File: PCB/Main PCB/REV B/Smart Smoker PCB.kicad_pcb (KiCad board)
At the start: 4 copper layers, 6.3 x 2.1 mm, 152 parts, among them J1 393570002, J10 Spare2, J2 Conn_01x03_Female, J3 1051330001, J4 Hopper, J5 393570002, J6 393570002, J7 Screen, J8 393570002, J9 Spare1, Q1 2N7002, Q2 2N7002, Q3 MBT3904DW1, Q4 2N7002, U1 AMS1117-3.3, U10 ALDP105W, U11 TLP2362TPR_E, U12 ALDP105W, U13 STM811SW16F, U2 TS5A23159DGS, U3 ESP32-WROOM-32UE_16MB, U4 MAX31855KASA, U5 TPS2115APWR, U6 TLP2362TPR_E, U7 ALDP105W, U8 CP2102N-A02-GQFN24, U9 TLP2362TPR_E

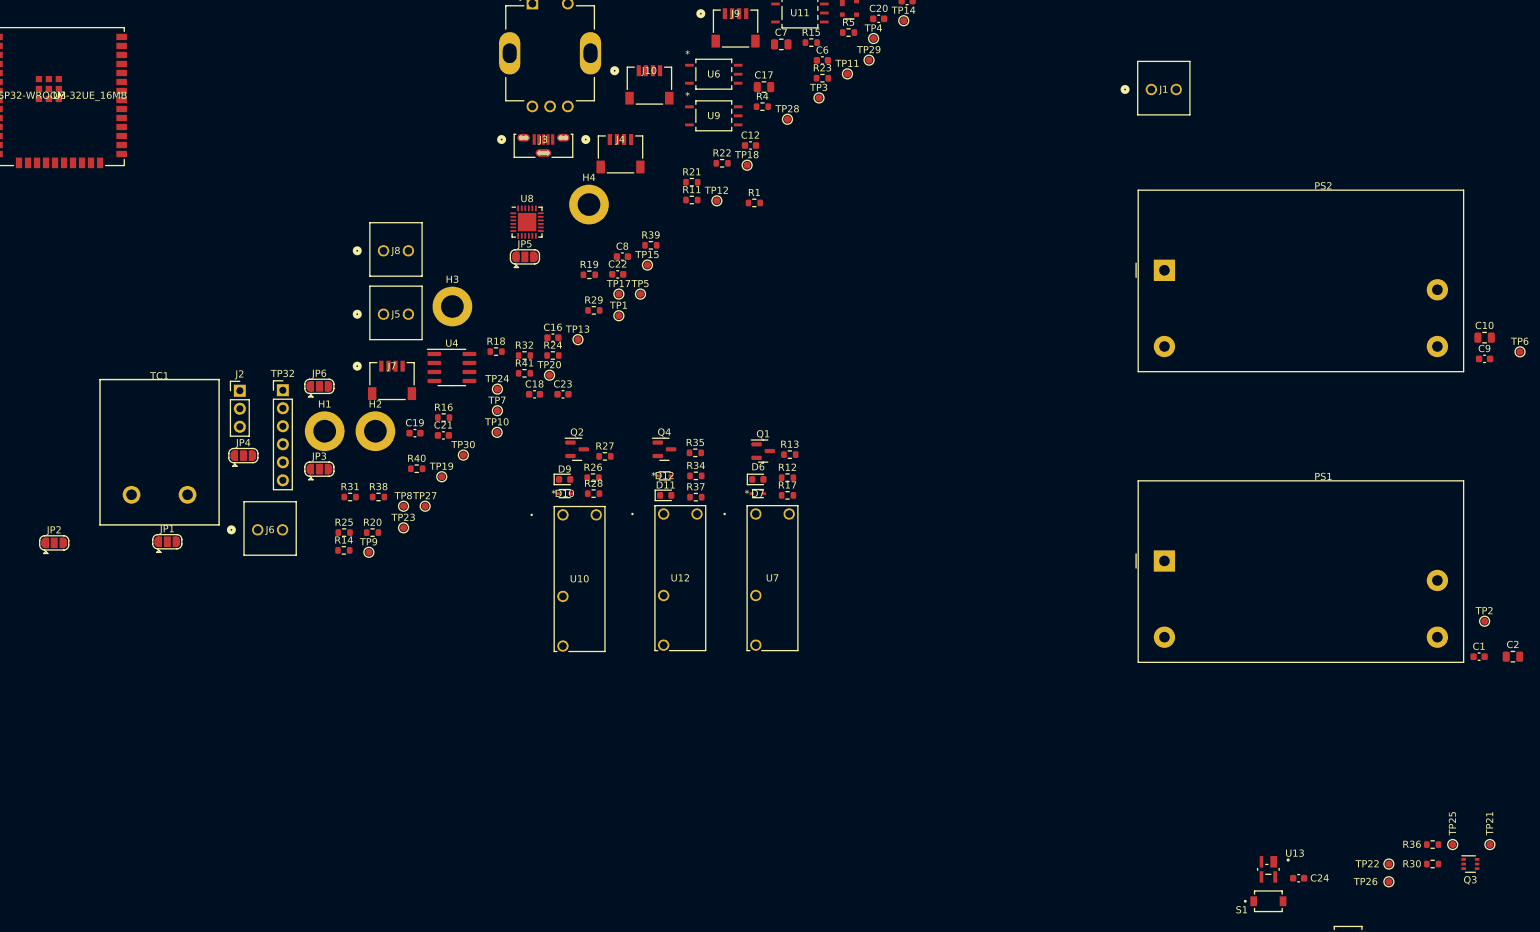
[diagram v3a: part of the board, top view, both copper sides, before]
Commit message: PCB Layout - Continue Grouping layout for relays
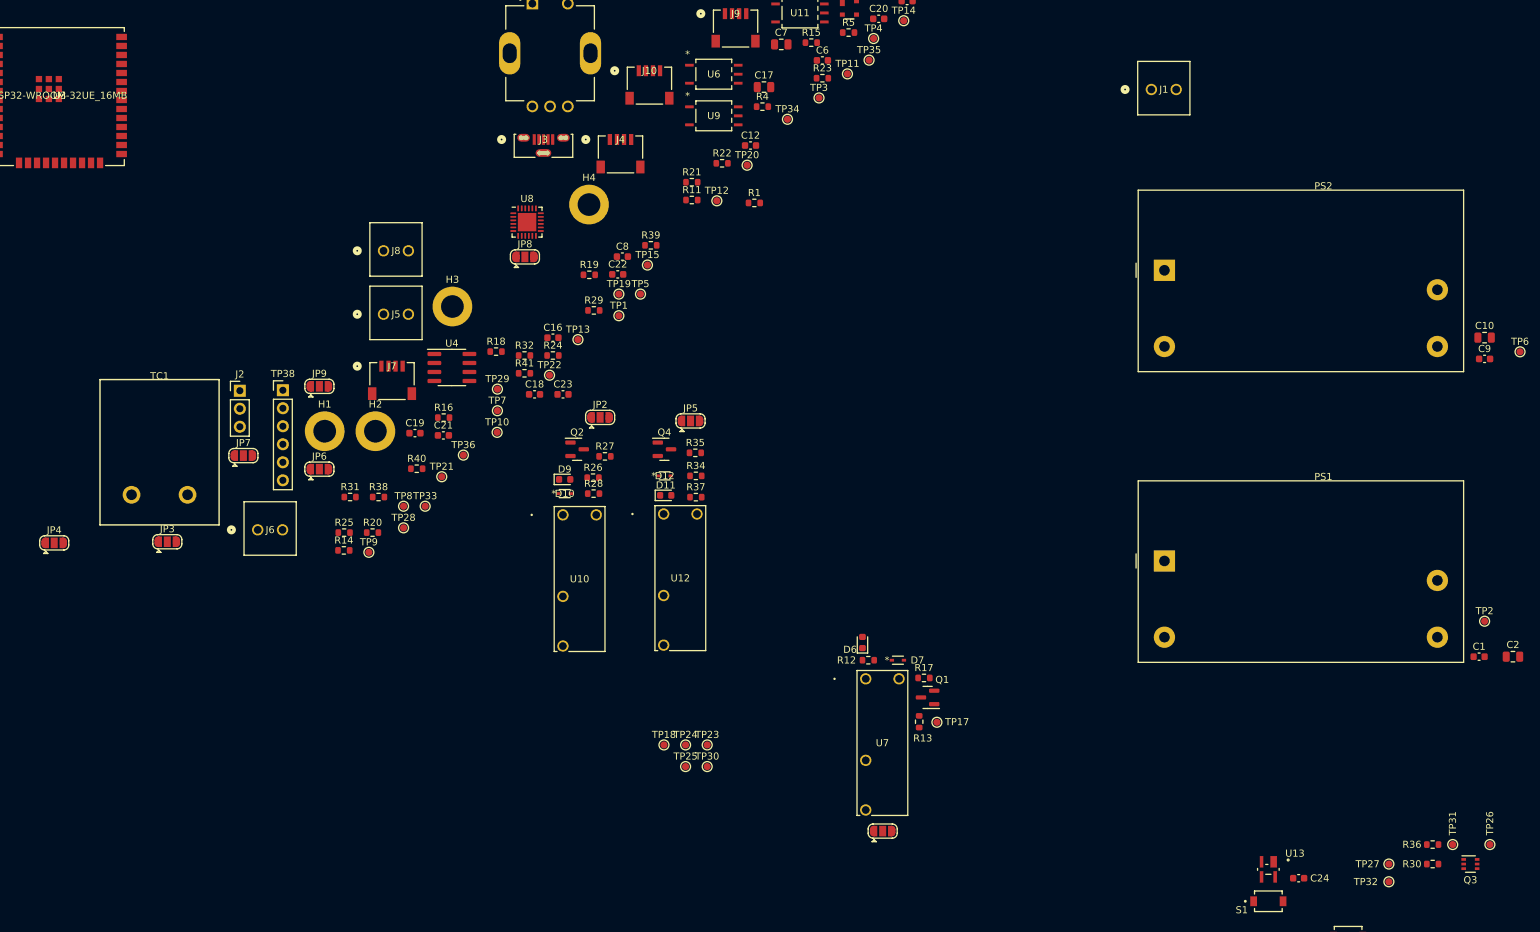
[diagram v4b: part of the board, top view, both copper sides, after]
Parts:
- added JP1: SolderJumper_3_Open, Jumper:SolderJumper-3_P1.3mm_Open_RoundedPad1.0x1.5mm, F.Cu at (148.1, 132.6)
- added JP2: SolderJumper_3_Open, Jumper:SolderJumper-3_P1.3mm_Open_RoundedPad1.0x1.5mm, F.Cu at (108.2, 74.2)
- added JP5: SolderJumper_3_Open, Jumper:SolderJumper-3_P1.3mm_Open_RoundedPad1.0x1.5mm, F.Cu at (121.0, 74.8)
- added TP17: TP, TestPoint:TestPoint_Pad_D1.0mm, F.Cu at (155.8, 117.2)
- added TP18: TP, TestPoint:TestPoint_Pad_D1.0mm, F.Cu at (117.2, 120.5)
- added TP23: TP, TestPoint:TestPoint_Pad_D1.0mm, F.Cu at (123.3, 120.5)
- added TP24: TP, TestPoint:TestPoint_Pad_D1.0mm, F.Cu at (120.3, 120.5)
- added TP25: TP, TestPoint:TestPoint_Pad_D1.0mm, F.Cu at (120.3, 123.5)
- added TP30: TP, TestPoint:TestPoint_Pad_D1.0mm, F.Cu at (123.3, 123.5)
- moved R13 41.9 mm to (153.2, 117.2), turned to 90 degrees
- moved Q1 41.8 mm to (154.4, 113.8), turned to 180 degrees
- moved R17 32.2 mm to (153.9, 111.0)
- moved D7 30.7 mm to (150.2, 108.5)
- moved R12 28.2 mm to (146.1, 108.5), turned to 180 degrees
- moved U7 27.9 mm to (145.7, 111.1)
- moved D6 27.3 mm to (145.2, 106.0), turned to 90 degrees
- renumbered JP1 to JP3, JP2 to JP4, JP3 to JP6, JP4 to JP7, JP5 to JP8, JP6 to JP9, TP17 to TP19, TP18 to TP20, TP19 to TP21, TP20 to TP22, TP21 to TP26, TP22 to TP27, TP23 to TP28, TP24 to TP29, TP25 to TP31, TP26 to TP32, TP27 to TP33, TP28 to TP34, TP29 to TP35, TP30 to TP36, TP32 to TP38
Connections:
- R13 pad 1: unconnected-(R13-Pad1) -> Net-(R13-Pad1)
- R15 pad 1: /AUGER -> /Auger
- R23 pad 1: /FAN -> /Fan
- R27 pad 1: unconnected-(R27-Pad1) -> Net-(R27-Pad1)
- R29 pad 1: /IGNITOR -> /Ignitor
- R35 pad 1: unconnected-(R35-Pad1) -> Net-(R35-Pad1)
- U3 pad 23: /IO15 -> /Auger
- U3 pad 26: /IO4 -> /Fan
- U3 pad 37: /IO23 -> /Ignitor

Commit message: PCB Layout - Set board outline and organize
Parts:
- removed J3: 1051330001, Customs Smoker:1051330001_MOL
- moved C1 243.8 mm to (291.3, -128.5)
- moved C10 243.8 mm to (292.1, -173.5)
- moved C11 243.8 mm to (210.6, -221.0)
- moved C12 243.8 mm to (188.5, -200.6)
- moved C13 243.8 mm to (317.8, -174.5)
- moved C14 243.8 mm to (317.8, -172.5)
- moved C15 243.8 mm to (318.1, -170.5)
- moved C16 243.8 mm to (160.6, -173.5)
- moved C17 243.8 mm to (190.4, -208.8)
- moved C18 243.8 mm to (158.1, -165.5)
- moved C19 243.8 mm to (141.2, -160.0)
- moved C2 243.8 mm to (296.1, -128.5)
- moved C20 243.8 mm to (206.6, -218.5)
- moved C21 243.8 mm to (145.2, -159.7)
- moved C22 243.8 mm to (169.8, -182.4)
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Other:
- board size 6.3 x 2.1 mm -> 60 x 120 mm

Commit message: PCB Layout - Modify board layout and get relay circuit organized
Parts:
- added J3: 1051330001, Customs Smoker:1051330001_MOL, F.Cu at (188.0, 33.5)
- moved C13 397.0 mm to (135.2, 178.0)
- moved C14 397.0 mm to (135.2, 180.0)
- moved C15 397.0 mm to (135.4, 182.0)
- moved C3 397.0 mm to (148.4, 162.0)
- moved C4 397.0 mm to (152.4, 162.0)
- moved C5 397.0 mm to (156.4, 162.0)
- moved D1 397.0 mm to (120.0, 151.0)
- moved D2 397.0 mm to (120.0, 157.0)
- moved D3 397.0 mm to (120.0, 153.0)
- moved D4 397.0 mm to (120.0, 159.0)
- moved D5 397.0 mm to (119.8, 155.0)
- moved R10 397.0 mm to (131.4, 176.0)
- moved R2 397.0 mm to (125.8, 151.0)
- moved R3 397.0 mm to (126.0, 157.0)
- moved R6 397.0 mm to (126.0, 153.0)
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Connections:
- J5 pad 2: /Auger_- -> /AC_N
- J6 pad 2: /Fan_- -> /AC_N
- J8 pad 2: /Ignitor_- -> /AC_N

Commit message: PCB Layout - Modify board layout and get relay circuit organized
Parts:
- moved R33 258.5 mm to (256.5, 57.8)
- moved U3 258.5 mm to (270.5, 63.8)
- moved C24 221.0 mm to (239.3, 140.2)
- moved C25 221.0 mm to (246.2, 151.5)
- moved Q3 221.0 mm to (263.5, 138.2)
- moved R30 221.0 mm to (258.2, 138.2)
- moved R36 221.0 mm to (258.2, 135.5)
- moved S1 221.0 mm to (235.0, 143.5)
- moved S2 221.0 mm to (246.2, 148.5)
- moved TP26 221.0 mm to (266.2, 135.5)
- moved TP27 221.0 mm to (252.0, 138.2)
- moved TP31 221.0 mm to (261.0, 135.5)
- moved TP32 221.0 mm to (252.0, 140.8)
- moved U13 221.0 mm to (235.0, 139.0)
- moved U11 187.5 mm to (58.5, 106.2), turned to -90 degrees
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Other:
- board size 60 x 120 mm -> 100 x 100 mm

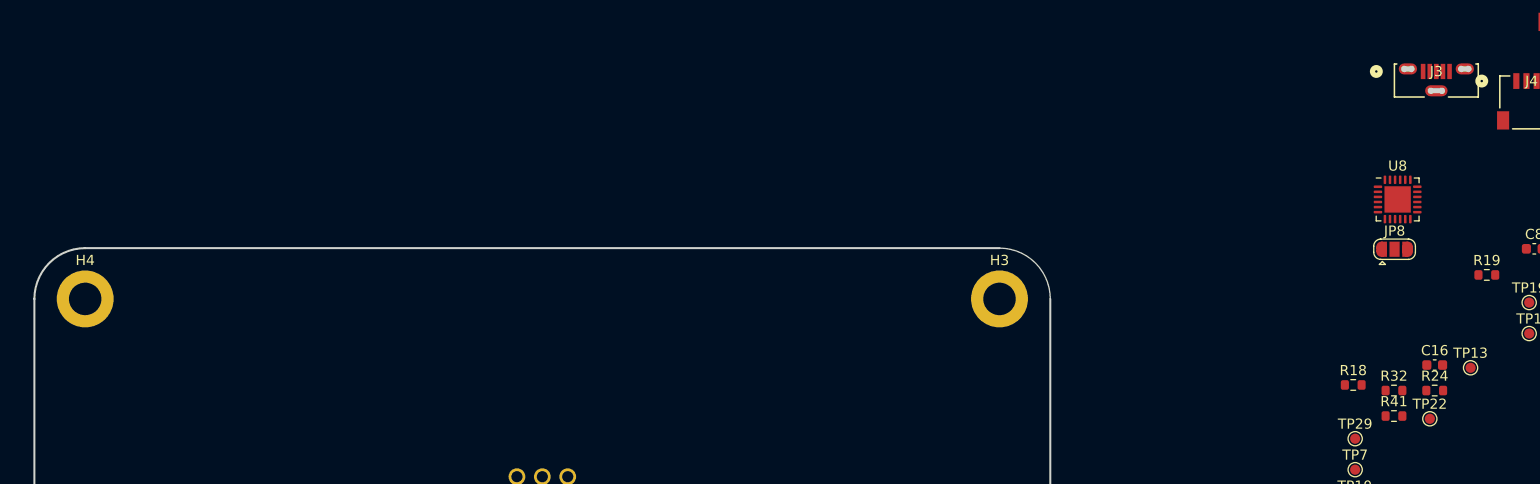
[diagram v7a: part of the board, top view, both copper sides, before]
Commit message: PCB Layout - Fix Usb footprint
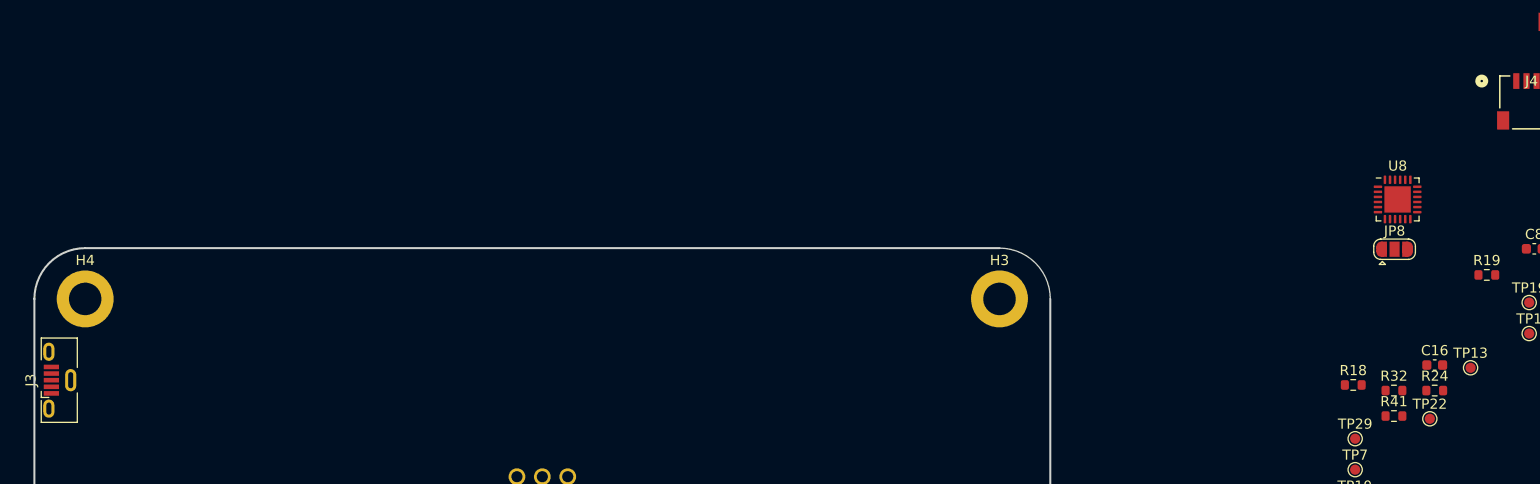
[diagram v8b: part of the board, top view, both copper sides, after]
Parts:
- J3: footprint Customs Smoker:1051330001_MOL -> Connector_USB:USB_Micro-B_Molex-105133-0001
- moved J3 138.7 mm to (52.5, 63.0), turned to 90 degrees
